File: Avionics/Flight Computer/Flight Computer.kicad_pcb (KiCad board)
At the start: 4 copper layers, 50 x 40 mm, 175 parts, among them J1 ERF8-040-05.0-S-DV-K, J2 ERF8-040-05.0-S-DV-K, J3 473460001, J4 734120110, J5 0734120110, J6 734120110, U1 CC1310F128RGZR, U12 ATSAME70Q21A-AN, U2 CC1190RGVR, U3 CC2650F128RGZR, U4 CC2592RGVR, U5 MPU-9250, U7 LPS25HB, U8 MAX17243, U9 MAX-M8W, Y1 9HT11-32.768KDZB-T, Y2 7V-16.000MAHJ-T, Y3 XRCGB24M000F2P00R0, Y5 XRCGB24M000F2P00R0

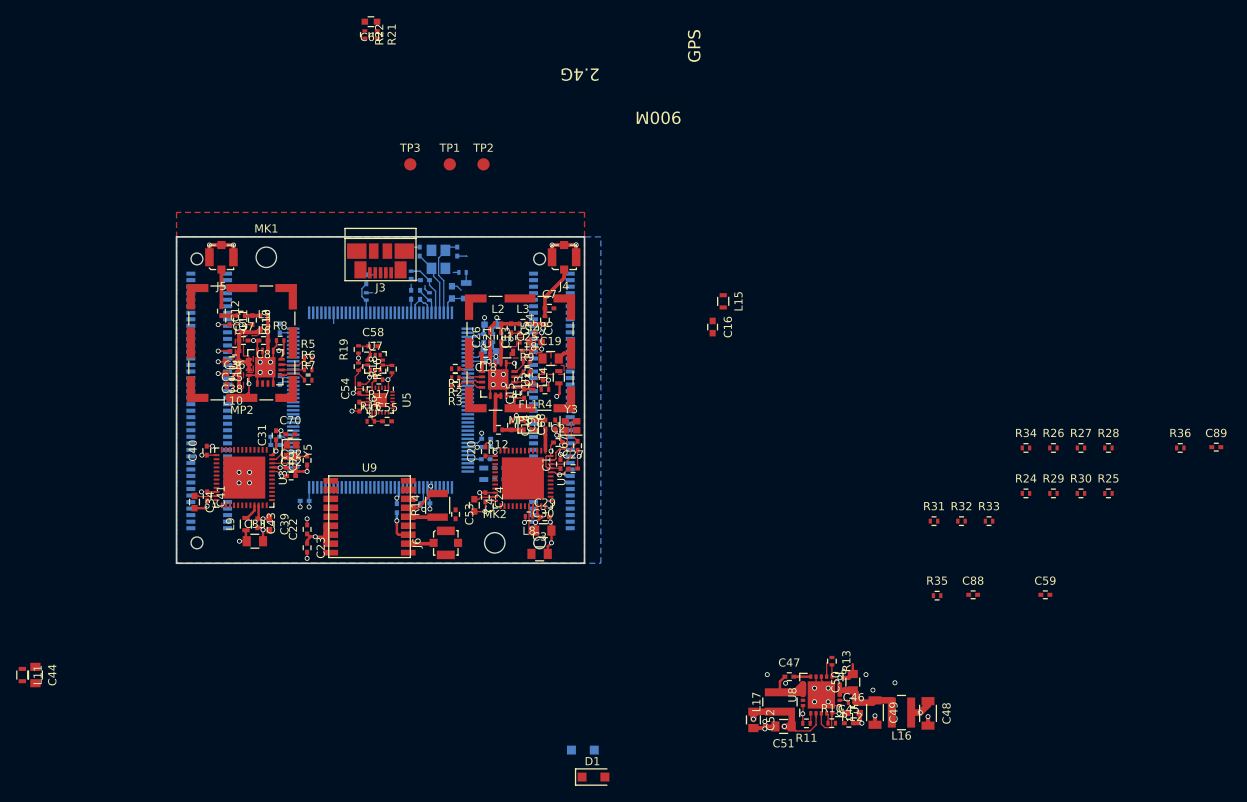
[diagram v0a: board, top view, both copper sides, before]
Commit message: Swapped some pins to make routing easier.
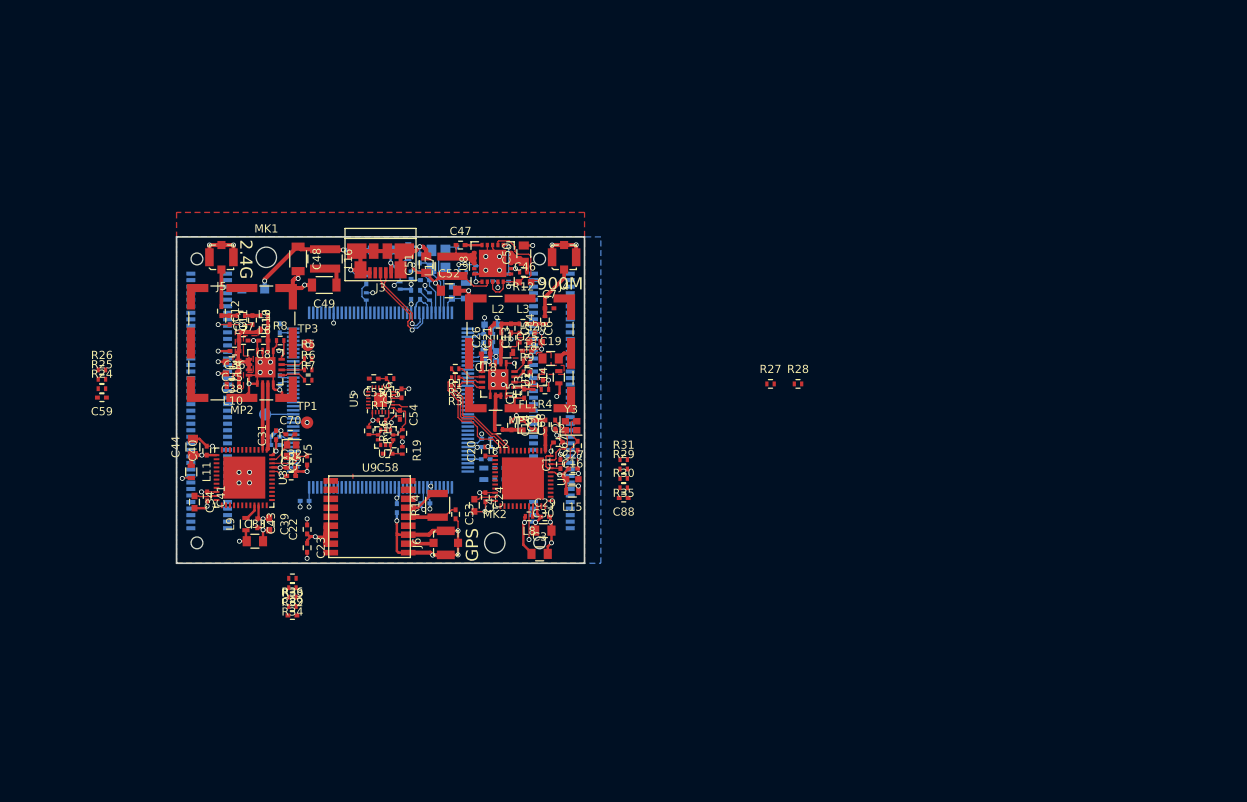
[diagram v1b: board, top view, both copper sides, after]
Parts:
- C45, C61, D1, R10, R11, R13, R21, R22, TP2: moved to B.Cu
- moved R25 124.2 mm to (40.9, 102.4)
- moved C59 118.1 mm to (40.9, 104.7), turned to 180 degrees
- moved R26 117.0 mm to (40.9, 101.3)
- moved C89 115.1 mm to (64.2, 131.4)
- moved R24 114.0 mm to (40.9, 103.6)
- moved R36 110.5 mm to (64.2, 130.3)
- moved C48 95.2 mm to (64.9, 87.7)
- moved R34 91.7 mm to (64.2, 129.1), turned to 180 degrees
- moved L16 89.9 mm to (68.2, 87.7), turned to 270 degrees
- moved R33 85.7 mm to (64.2, 126.8), turned to 180 degrees
- moved C49 85.5 mm to (68.1, 90.9), turned to 180 degrees
- moved R32 82.4 mm to (64.2, 128.0), turned to 180 degrees
- moved C51 71.6 mm to (80.6, 88.4), turned to 90 degrees
- moved C45 71.5 mm to (88.8, 87.9), turned to 90 degrees
- moved D1 69.5 mm to (75.4, 86.6)
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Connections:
- U1 pad 10: /900MHz Radio/LNA_EN -> /900MHz Radio/HGM
- U1 pad 12: /900MHz Radio/HGM -> /900MHz Radio/LNA_EN
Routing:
- net GND: track 160.8 -> 215.5 mm, vias 62 -> 70
- net /900MHz Radio/HGM: track 0.10 -> 14.0 mm
- net Net-(C48-Pad1): track 2.91 -> 16.2 mm, vias 1 -> 2
- net /900MHz Radio/LNA_EN: track 0.10 -> 13.4 mm
- net /Connectors/USBD_P: track 0.00 -> 11.7 mm, vias 0 -> 1
- net /900MHz Radio/PA_EN: track 0.07 -> 11.6 mm
- net /Connectors/USBD_N: track 0.00 -> 10.1 mm, vias 0 -> 1
- net /2.4 GHz Radio/RF50_2.4_P: track 0.00 -> 8.16 mm
- net /2.4 GHz Radio/RF50_2.4_N: track 0.00 -> 8.12 mm
- net /Power/BIAS: track 8.15 -> 15.0 mm, vias 1 -> 0
- net VUSB: track 0.00 -> 5.97 mm, vias 0 -> 1
- net /900MHz Radio/VDDR_CC1310: track 6.62 -> 10.9 mm
- net /900MHz Radio/VDDS_CC1310: track 11.6 -> 15.6 mm
- net /Connectors/PB12: track 0.00 -> 3.45 mm
- net +3V3: track 46.1 -> 48.9 mm, vias 10 -> 14
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
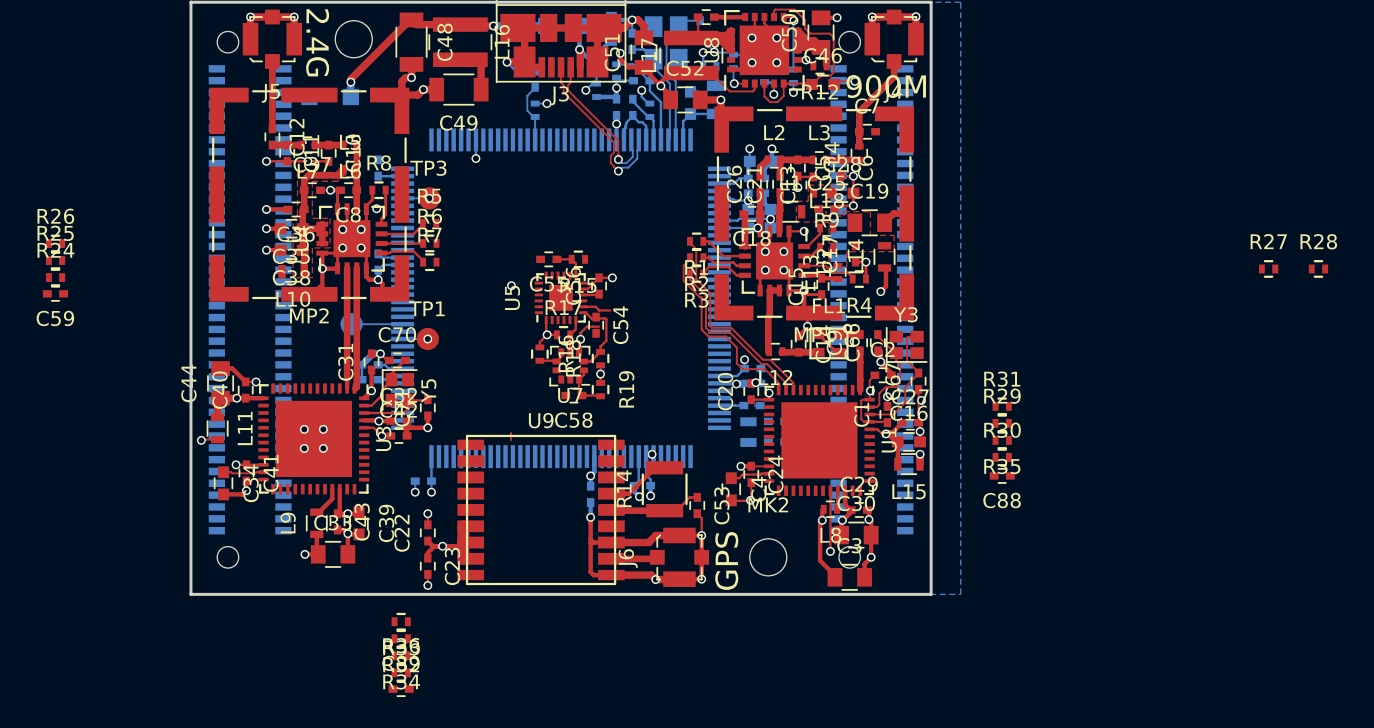
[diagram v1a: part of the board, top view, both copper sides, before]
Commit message: Some more pin swapping and routing of signals. Placed reset pullup resistors.
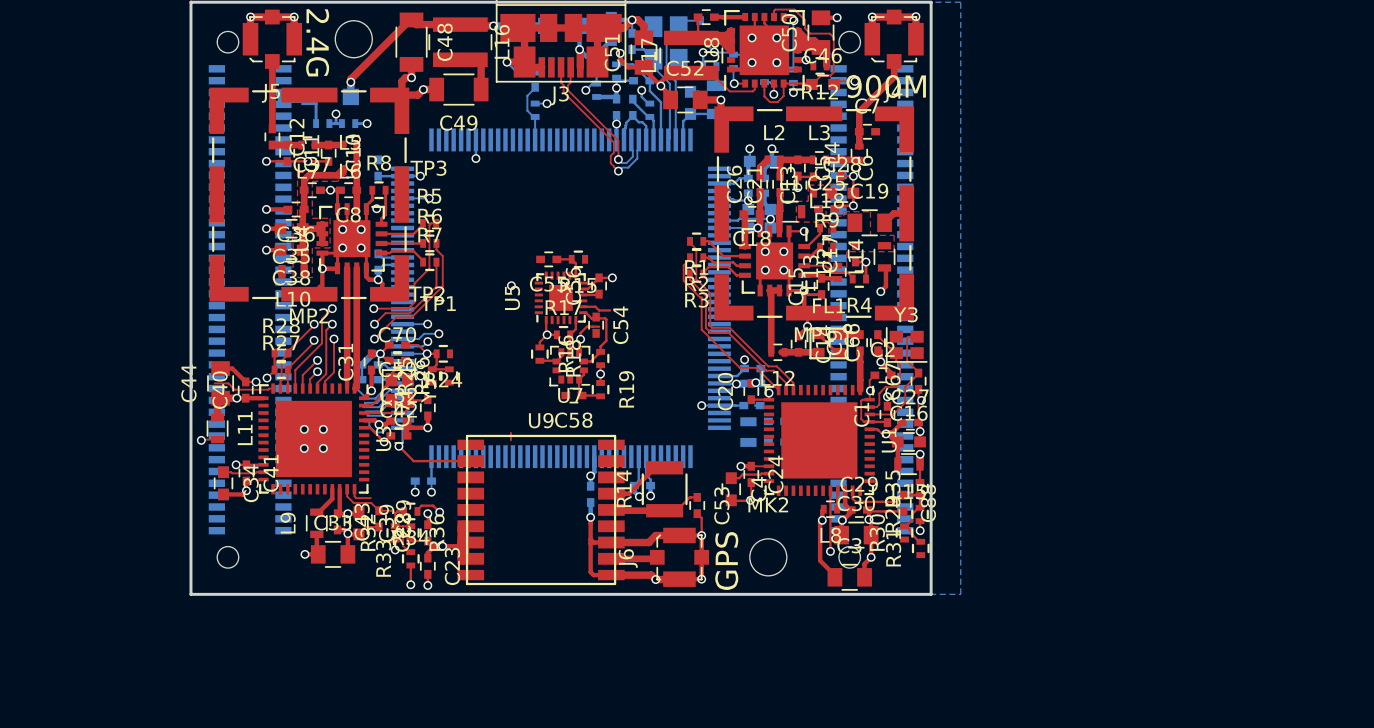
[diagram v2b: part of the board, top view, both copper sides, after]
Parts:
- added R37: 100k, Resistors_SMD:R_0402, B.Cu at (58.9, 93.2)
- added R38: 10k, Resistors_SMD:R_0402, B.Cu at (60.7, 93.2)
- TP1, TP3: footprint Measurement_Points:Measurement_Point_Round-SMD-Pad_Small -> Measurement_Points:Measurement_Point_Round-SMD-Pad_Very_Small
- TP2: footprint Measurement_Points:Measurement_Point_Round-SMD-Pad_Small -> Measurement_Points:Measurement_Point_Round-SMD-Pad_Very_Small; moved to F.Cu
- moved R28 70.3 mm to (56.1, 108.7)
- moved R27 67.0 mm to (56.1, 109.8)
- moved R26 28.1 mm to (67.5, 110.2), turned to 90 degrees
- moved R24 26.7 mm to (67.1, 108.7), turned to 180 degrees
- moved R25 26.6 mm to (66.3, 110.2), turned to 90 degrees
- moved C59 23.4 mm to (64.0, 108.1)
- moved C89 11.6 mm to (62.7, 119.9), turned to 270 degrees
- moved R31 11.1 mm to (99.3, 121.9), turned to 90 degrees
- moved R34 9.77 mm to (64.9, 119.4)
- moved R36 9.47 mm to (64.9, 120.8), turned to 270 degrees
- moved R30 8.34 mm to (98.2, 120.8), turned to 90 degrees
- moved R29 8.28 mm to (99.3, 119.6), turned to 90 degrees
- moved R32 7.16 mm to (63.8, 120.8), turned to 90 degrees
- moved C88 6.90 mm to (98.2, 118.8), turned to 270 degrees
- moved R35 6.43 mm to (99.3, 117.8), turned to 90 degrees
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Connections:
- net /GNC_Processor/PD31 renamed /Connectors/PD31
- J1 pad 5: Net-(J1-Pad5) -> +BATT
- J1 pad 7: Net-(J1-Pad7) -> +BATT
- U12 pad 34: /GNC_Processor/PD30 -> /GNC_Processor/VBATT
- U3 pad 5: /2.4 GHz Radio/PA_EN -> /2.4 GHz Radio/LNA_EN
- U3 pad 6: /2.4 GHz Radio/LNA_EN -> /2.4 GHz Radio/PA_EN
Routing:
- net /2.4 GHz Radio/HGM: track 0.00 -> 18.3 mm, vias 0 -> 2
- net /2.4 GHz Radio/LNA_EN: track 0.00 -> 15.5 mm, vias 0 -> 2
- net /2.4 GHz Radio/PA_EN: track 0.00 -> 14.5 mm, vias 0 -> 2
- net /900MHz Radio/~RESET: track 0.00 -> 9.54 mm
- net /2.4 GHz Radio/~RESET: track 0.00 -> 8.75 mm
- net /CPU-SCK: track 0.00 -> 8.21 mm, vias 0 -> 1
- net /GPS/GPS-Tx: track 0.00 -> 6.62 mm, vias 0 -> 1
- net /GNC_Processor/~RESET: track 0.00 -> 6.32 mm, vias 0 -> 1
- net +3V3: track 48.9 -> 54.8 mm, vias 14 -> 16
- net GND: track 215.5 -> 221.0 mm, vias 70 -> 71
- net /2.4G-Tx: track 0.00 -> 4.78 mm, vias 0 -> 1
- net +BATT: track 0.00 -> 4.58 mm
- net /2.4 GHz Radio/DIO-7: track 0.00 -> 4.16 mm
- net /GNC_Processor/PB6: track 0.00 -> 4.09 mm
- net /CPU-SDA: track 0.00 -> 3.99 mm, vias 0 -> 1
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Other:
- net class RF_50Ohm: clearance 0.16 -> 0.25

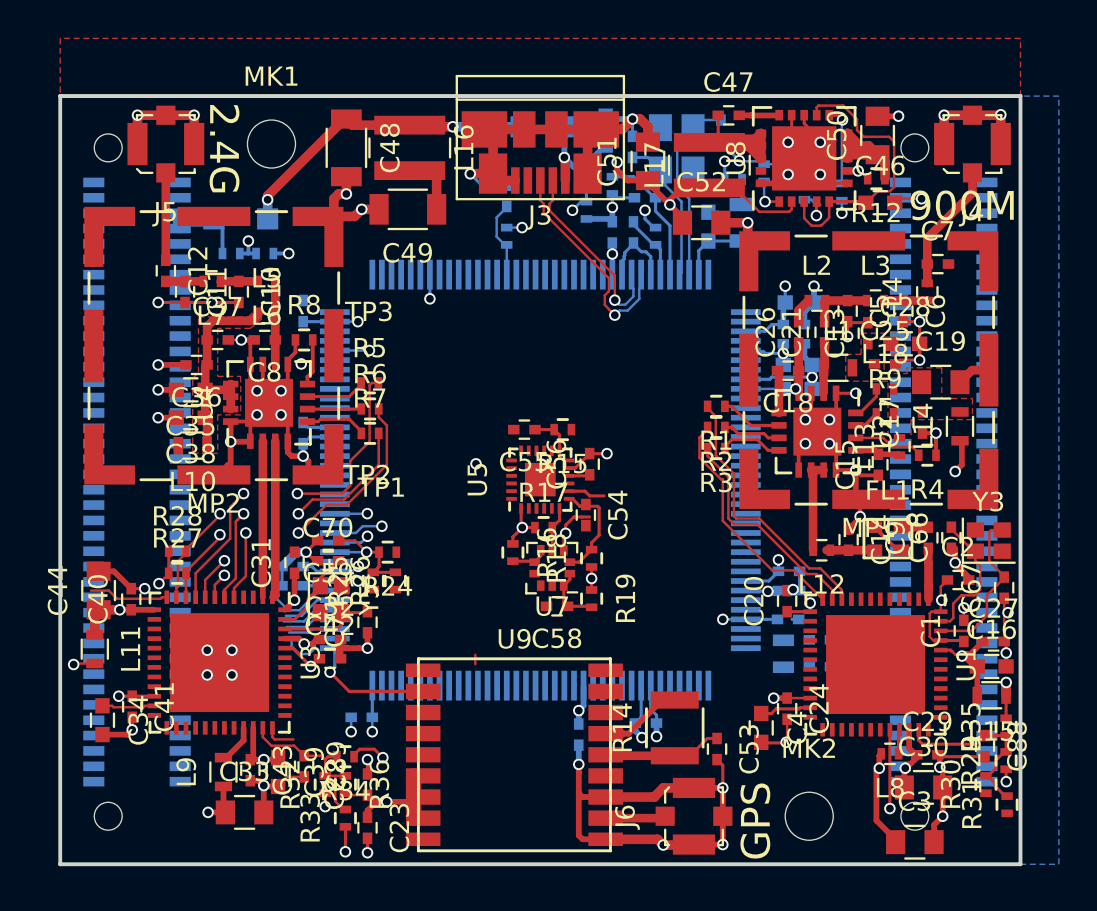
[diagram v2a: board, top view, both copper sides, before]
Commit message: Cleaned up vias and DRC Errors
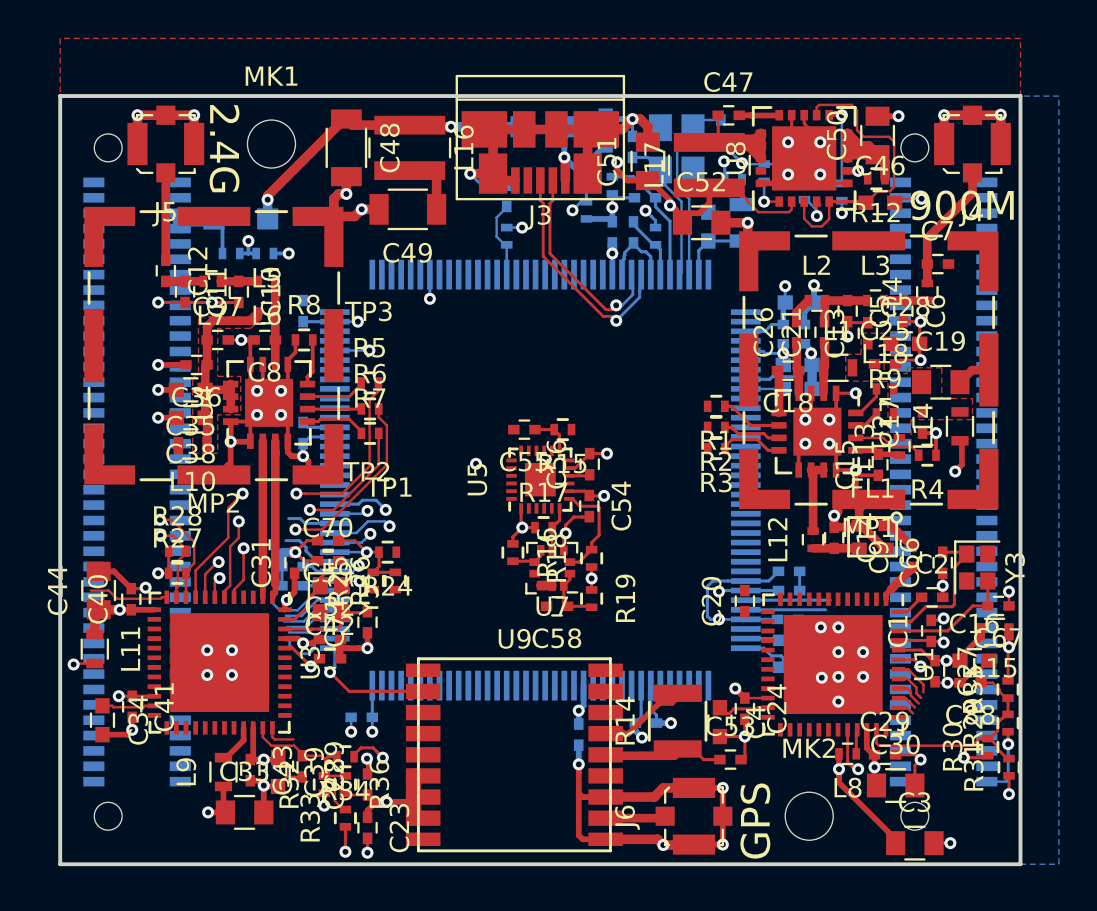
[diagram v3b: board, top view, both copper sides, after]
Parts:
- moved C27 3.42 mm to (95.5, 115.0), turned to 270 degrees
- moved C88 3.38 mm to (97.4, 115.5), turned to 180 degrees
- moved L15 3.30 mm to (98.7, 112.9)
- moved C20 2.20 mm to (85.7, 111.3)
- moved C29 2.20 mm to (93.0, 119.3)
- moved L8 2.20 mm to (91.0, 119.2)
- moved C24 2.20 mm to (85.7, 116.9)
- moved U1 2.20 mm to (90.3, 114.6)
- moved C4 2.17 mm to (84.3, 117.6)
- moved R29 1.95 mm to (99.4, 117.6)
- moved R30 1.95 mm to (98.3, 118.9)
- moved R35 1.95 mm to (99.4, 115.9)
- moved R31 1.95 mm to (99.4, 119.9)
- moved C1 1.70 mm to (95.3, 112.8)
- moved C2 1.62 mm to (95.4, 111.1)
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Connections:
- J2 pad 63: Net-(J2-Pad63) -> /Connectors/900-ADIO-30
- J2 pad 65: Net-(J2-Pad65) -> /Connectors/900-ADIO-29
- J2 pad 67: Net-(J2-Pad67) -> /Connectors/900-ADIO-28
- J2 pad 69: Net-(J2-Pad69) -> /Connectors/900-ADIO-26
- J2 pad 71: Net-(J2-Pad71) -> /Connectors/900-ADIO-23
- J2 pad 73: Net-(J2-Pad73) -> /Connectors/900-ADIO-24
- J2 pad 75: Net-(J2-Pad75) -> /Connectors/900-ADIO-25
- J2 pad 77: Net-(J2-Pad77) -> /Connectors/900-ADIO-27
- J2 pad 79: Net-(J2-Pad79) -> /900_RESET_EXT
- U1 pad 36: /900MHz Radio/ADIO-23 -> /Connectors/900-ADIO-23
- U1 pad 37: /900MHz Radio/ADIO-24 -> /Connectors/900-ADIO-24
- U1 pad 38: /900MHz Radio/ADIO-25 -> /Connectors/900-ADIO-25
- U1 pad 39: /900MHz Radio/ADIO-26 -> /Connectors/900-ADIO-26
- U1 pad 40: /900MHz Radio/ADIO-27 -> /Connectors/900-ADIO-27
- U1 pad 41: /900MHz Radio/ADIO-28 -> /Connectors/900-ADIO-28
- U1 pad 42: /900MHz Radio/ADIO-29 -> /Connectors/900-ADIO-29
- U1 pad 43: /900MHz Radio/ADIO-30 -> /Connectors/900-ADIO-30
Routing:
- net /900MHz Radio/HGM: track 14.0 -> 0.10 mm
- net /900MHz Radio/LNA_EN: track 12.5 -> 0.10 mm
- net /900MHz Radio/PA_EN: track 11.6 -> 0.07 mm
- net /GNC_Processor/PB3: track 0.00 -> 4.40 mm
- net GND: track 221.0 -> 225.3 mm, vias 71 -> 78
- net /GNC_Processor/PA21: track 0.00 -> 4.15 mm
- net Net-(C63-Pad2): track 0.00 -> 4.00 mm
- net /900_RESET_CPU: track 0.00 -> 3.89 mm, vias 0 -> 2
- net Net-(C57-Pad1): track 19.4 -> 23.3 mm, vias 8 -> 7
- net /900MHz Radio/~RESET: track 9.54 -> 13.0 mm
- net Net-(C62-Pad2): track 0.00 -> 3.36 mm
- net /900MHz Radio/VDDS_CC1310: track 15.6 -> 12.4 mm
- net /GNC_Processor/PC8: track 0.00 -> 3.11 mm
- net /900_RESET_EXT: track 0.65 -> 3.66 mm
- net /GNC_Processor/PC9: track 0.00 -> 2.50 mm
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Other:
- net class Default: trace_width 0.2 -> 0.16; via_dia 0.6 -> 0.625; via_drill 0.4 -> 0.305
- net class RF_50Ohm: clearance 0.25 -> 0.16; via_dia 0.6 -> 0.625; via_drill 0.4 -> 0.305
- net class USB_Data: trace_width 0.2 -> 0.16; via_dia 0.6 -> 0.625; via_drill 0.4 -> 0.305
- rule via_min_size: 0.465 -> 0.625
